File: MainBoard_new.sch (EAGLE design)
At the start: 57 parts, among them U1 STM32F10XRXT6, Y1 8MHz, Y2 32.768kHz

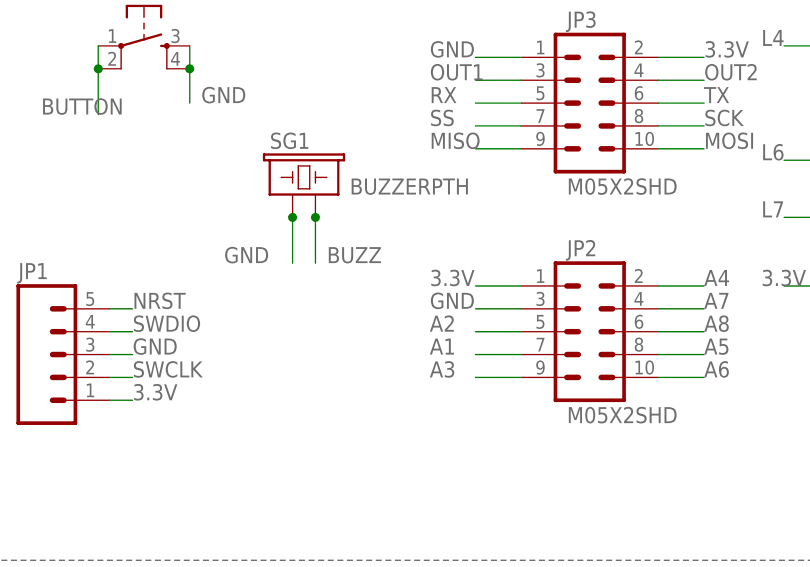
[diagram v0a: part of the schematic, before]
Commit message: kompresja płytki, dodany npn do buzzera
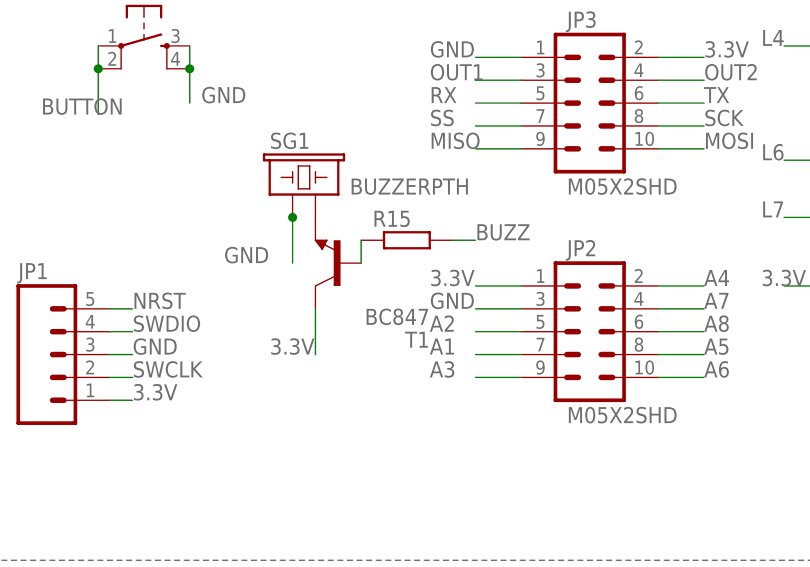
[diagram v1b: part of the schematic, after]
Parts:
- added R15: (no value), rcl:R-EU_R0805
- added T1: BC847, transistor:BC847
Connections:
- new net N$17: SG1.2, T1.E
- new net N$20: R15.1, T1.B
- net 3.3V: now also T1.C
- net BUZZ: now also R15.2; no longer SG1.2
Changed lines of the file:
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@@
 <part name="R9" library="resistor" deviceset="R-EU_" device="M0805"/>
 <part name="R11" library="resistor" deviceset="R-EU_" device="M0805"/>
+<part name="T1" library="transistor" deviceset="BC847" device=""/>
+<part name="R15" library="rcl" deviceset="R-EU_" device="R0805"/>
 </parts>
 <sheets>
@@
 <instance part="R9" gate="G$1" x="153.67" y="214.63" rot="R90"/>
 <instance part="R11" gate="G$1" x="153.67" y="204.47" rot="R90"/>
+<instance part="T1" gate="G$1" x="182.88" y="157.48" rot="R180"/>
+<instance part="R15" gate="G$1" x="190.5" y="160.02"/>
 </instances>
 <busses>
@@
 <wire x1="236.22" y1="154.94" x2="232.41" y2="154.94" width="0.1524" layer="91"/>
 <label x="229.87" y="154.94" size="1.778" layer="95"/>
+</segment>
+<segment>
+<pinref part="T1" gate="G$1" pin="C"/>
+<wire x1="180.34" y1="152.4" x2="180.34" y2="147.32" width="0.1524" layer="91"/>
+<label x="175.26" y="147.32" size="1.778" layer="95"/>
 </segment>
 </net>
@@
 <net name="BUZZ" class="0">
 <segment>
-<pinref part="SG1" gate="G$1" pin="2"/>
-<wire x1="180.34" y1="162.56" x2="180.34" y2="157.48" width="0.1524" layer="91"/>
-<label x="181.61" y="157.48" size="1.778" layer="95"/>
-<junction x="180.34" y="162.56"/>
-</segment>
-<segment>
 <wire x1="16.51" y1="58.42" x2="15.24" y2="58.42" width="0.1524" layer="91"/>
 <label x="1.27" y="58.42" size="1.778" layer="95"/>
@@
 <wire x1="15.24" y1="58.42" x2="8.89" y2="58.42" width="0.1524" layer="91"/>
 </segment>
+<segment>
+<pinref part="R15" gate="G$1" pin="2"/>
+<wire x1="195.58" y1="160.02" x2="198.12" y2="160.02" width="0.1524" layer="91"/>
+<label x="198.12" y="160.02" size="1.778" layer="95"/>
+</segment>
 </net>
 <net name="SS" class="0">
@@
 </segment>
 </net>
+<net name="N$17" class="0">
+<segment>
+<pinref part="SG1" gate="G$1" pin="2"/>
+<pinref part="T1" gate="G$1" pin="E"/>
+</segment>
+</net>
+<net name="N$20" class="0">
+<segment>
+<pinref part="T1" gate="G$1" pin="B"/>
+<wire x1="185.42" y1="157.48" x2="185.42" y2="160.02" width="0.1524" layer="91"/>
+<pinref part="R15" gate="G$1" pin="1"/>
+</segment>
+</net>
